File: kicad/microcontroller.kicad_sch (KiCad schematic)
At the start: 10 parts, among them J601 AVR-ISP-6, U601 ATtiny1634-S

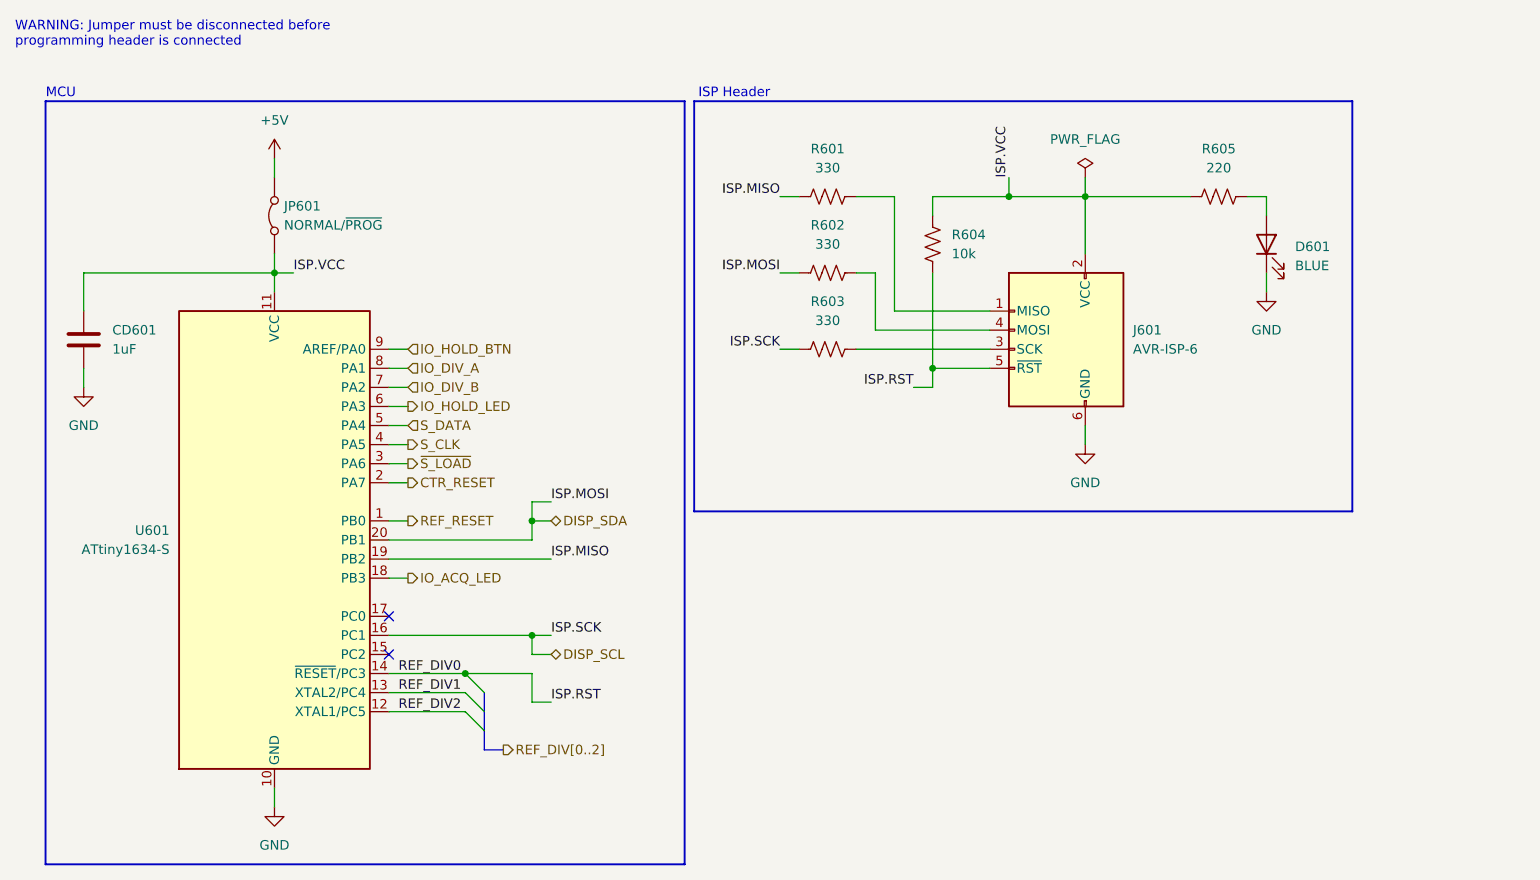
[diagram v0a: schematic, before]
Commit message: rework isp header, update pinout
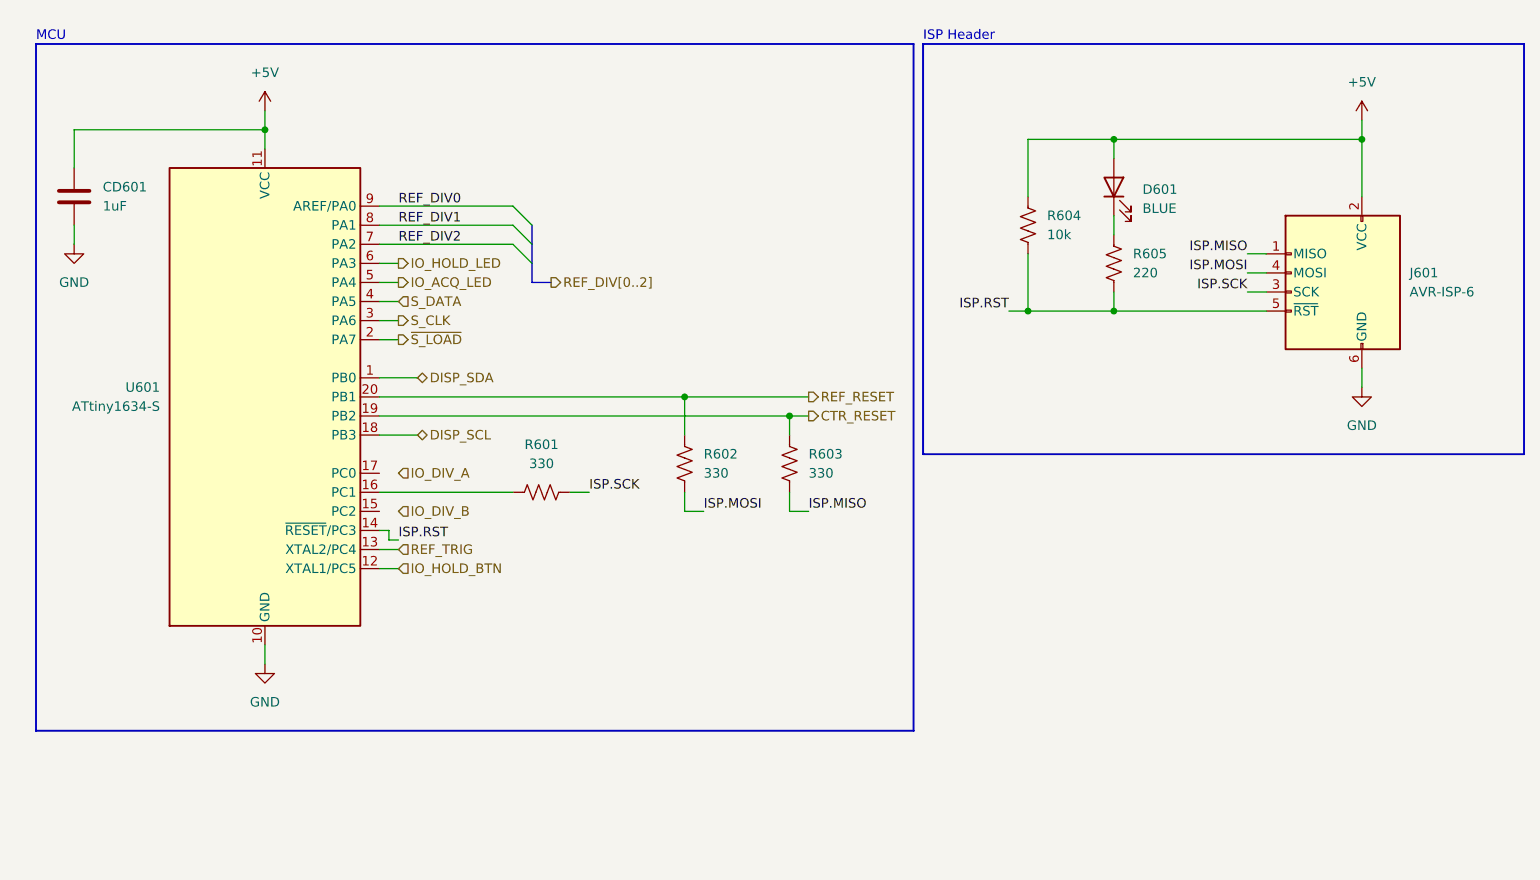
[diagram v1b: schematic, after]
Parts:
- removed JP601: NORMAL/~{PROG}, Custom:TestPoint_2Pads_Pitch2.54mm_Drill0.8mm_Fix, symbol Jumper:Jumper_2_Bridged
- renumbered R603 to R601, R601 to R602, R602 to R603
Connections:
- net +5V: now also CD601.1, D601.2 (A), J601.2 (VCC), R604.1, U601.11 (VCC)
- net CTR_RESET: now also R603.2, U601.19 (PB2); no longer U601.2 (PA7)
- net DISP_SCL: now also U601.18 (PB3); no longer R601.1, U601.16 (PC1)
- net DISP_SDA: now also U601.1 (PB0); no longer R603.1, U601.20 (PB1)
- net GND: no longer D601.1 (K)
- net IO_ACQ_LED: now also U601.5 (PA4); no longer U601.18 (PB3)
- net IO_DIV_A: no longer U601.8 (PA1)
- net IO_DIV_B: no longer U601.7 (PA2)
- net IO_HOLD_BTN: now also U601.12 (XTAL1/PC5); no longer U601.9 (AREF/PA0)
- net ISP.MISO: now also J601.1 (MISO), R603.1; no longer R602.1, U601.19 (PB2)
- net ISP.RST: now also R605.1
- net REF_DIV1: now also U601.8 (PA1); no longer U601.13 (XTAL2/PC4)
- net REF_DIV2: now also U601.7 (PA2); no longer U601.12 (XTAL1/PC5)
- net REF_RESET: now also R602.1, U601.20 (PB1); no longer U601.1 (PB0)
- net S_CLK: now also U601.3 (PA6); no longer U601.4 (PA5)
- net S_DATA: now also U601.4 (PA5); no longer U601.5 (PA4)
- net ~{S_LOAD}: now also U601.2 (PA7); no longer U601.3 (PA6)
- net ISP.MOSI: now reaches R602.2
- net ISP.MOSI: now also J601.4 (MOSI); no longer J601.1 (MISO)
- net at R601.2: now also U601.16 (PC1); no longer J601.3 (SCK)
- net at R605.2: now also D601.1 (K); no longer D601.2 (A)
- removed net ISP.VCC: CD601.1, J601.2 (VCC), R604.1, R605.1, U601.11 (VCC)
- new net ISP.SCK: J601.3 (SCK), R601.1
- new net REF_DIV0: U601.9 (AREF/PA0)
- new net REF_TRIG: U601.13 (XTAL2/PC4)
- no-connect marks 2 -> 0
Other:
- note removed: "WARNING: Jumper must be disconnected before programming header is connected"
- moved on the sheet: CD601, D601, J601, R601, R602, R603, R604, R605, U601

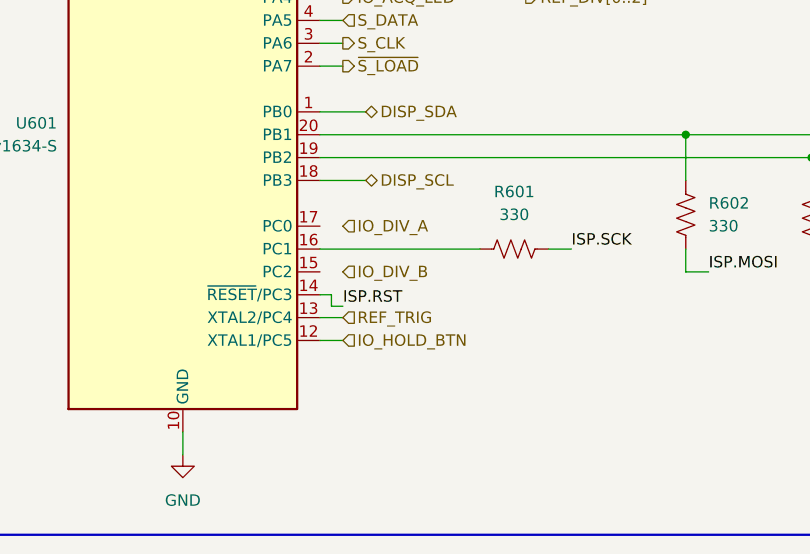
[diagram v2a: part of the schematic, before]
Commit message: swap encoder for two buttons, assign channel select pin
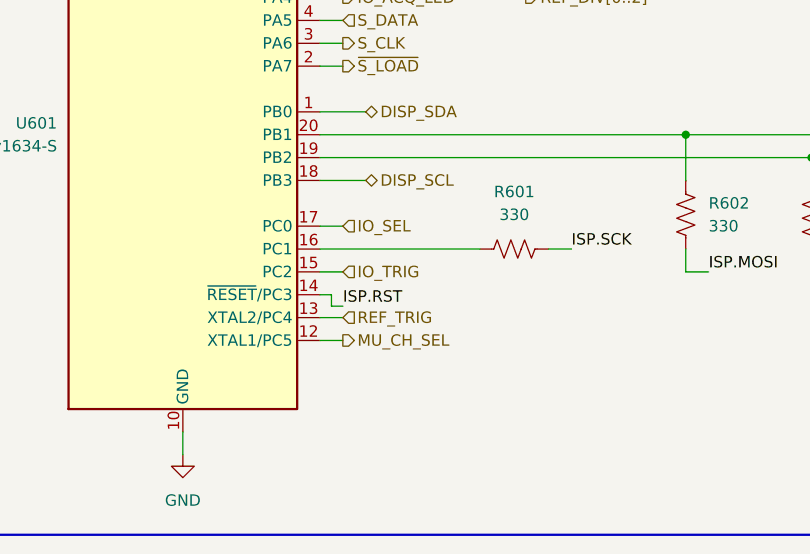
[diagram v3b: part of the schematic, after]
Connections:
- net IO_TRIG: now reaches U601.15 (PC2)
- net IO_SEL: now reaches U601.17 (PC0)
- net IO_HOLD_BTN renamed MU_CH_SEL
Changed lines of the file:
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@@
+	(wire
+		(pts
+			(xy 62.23 74.93) (xy 64.77 74.93)
+		)
+		(stroke
+			(width 0)
+			(type default)
+		)
+	)
 	(wire
 		(pts
@@
 		(pts
 			(xy 62.23 87.63) (xy 64.77 87.63)
+		)
+		(stroke
+			(width 0)
+			(type default)
+		)
+	)
+	(wire
+		(pts
+			(xy 62.23 80.01) (xy 64.77 80.01)
 		)
 		(stroke
@@
 		)
 	)
+	(hierarchical_label "MU_CH_SEL"
+		(shape output)
+		(at 64.77 87.63 0)
+		(effects
+			(font
+				(size 1.27 1.27)
+			)
+			(justify left)
+		)
+	)
 	(hierarchical_label "S_CLK"
 		(shape output)
@@
 		)
 	)
-	(hierarchical_label "IO_DIV_B"
+	(hierarchical_label "IO_TRIG"
 		(shape input)
 		(at 64.77 80.01 0)
@@
 		)
 	)
-	(hierarchical_label "IO_HOLD_BTN"
-		(shape input)
-		(at 64.77 87.63 0)
-		(effects
-			(font
-				(size 1.27 1.27)
-			)
-			(justify left)
-		)
-	)
 	(hierarchical_label "REF_DIV[0..2]"
 		(shape output)
@@
 		)
 	)
-	(hierarchical_label "IO_DIV_A"
+	(hierarchical_label "IO_SEL"
 		(shape input)
 		(at 64.77 74.93 0)

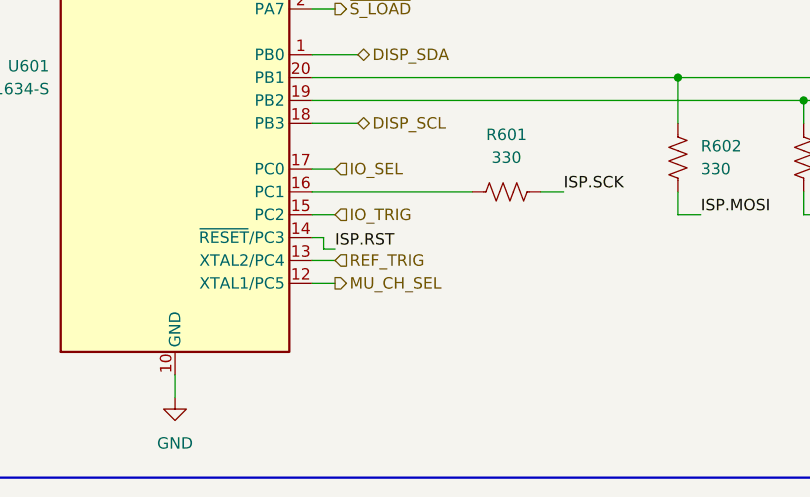
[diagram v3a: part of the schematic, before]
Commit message: rework frontend, channel gating
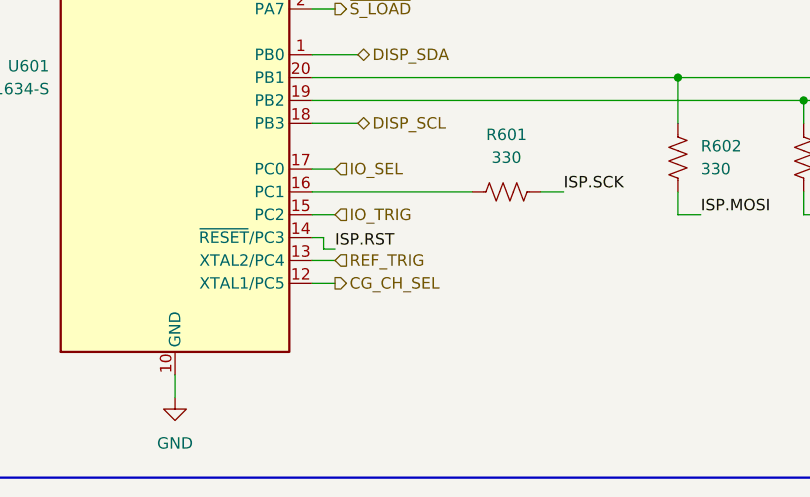
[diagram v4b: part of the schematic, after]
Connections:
- net MU_CH_SEL renamed CG_CH_SEL
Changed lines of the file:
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@@
 		)
 	)
-	(hierarchical_label "MU_CH_SEL"
+	(hierarchical_label "CG_CH_SEL"
 		(shape output)
 		(at 64.77 87.63 0)

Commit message: replace alum caps with ceramics, change mpn labeling
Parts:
- CD601: MPN (none) -> 0402ZD105KAT2A; Supplier https://www.digikey.com/en/products/detail/kyocera-avx/0402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 -> (none)
- D601: MPN (none) -> E1221NB--05D000814U1930; Supplier https://www.digikey.com/en/products/detail/harvatek-corpora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 -> (none)
- J601: Supplier Generic -> (none)
- R601, R602, R603: MPN (none) -> RC0402JR-13330RL; Supplier https://www.digikey.com/en/products/detail/yageo/RC0402JR-1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 -> (none)
- R604: MPN (none) -> RC0402JR-1310KL; Supplier https://www.digikey.com/en/products/detail/yageo/RC0402JR-1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 -> (none)
- R605: MPN (none) -> RC0402JR-13220RL; Supplier https://www.digikey.com/en/products/detail/yageo/RC0402JR-1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 -> (none)
- U601: MPN (none) -> ATTINY1634-SU; Supplier https://www.digikey.com/en/products/detail/microchip-techno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 -> (none)
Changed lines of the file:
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@@
 			)
 		)
-		(property "Supplier" "Generic"
+		(property "Supplier" ""
 			(at 190.5 50.8 0)
 			(effects
@@
 			)
 		)
-		(property "Supplier" "https://www.digikey.com/en/products/detail/yageo/RC0402JR-13220RL/14008194"
+		(property "Supplier" ""
 			(at 160.02 46.99 90)
+			(effects
+				(font
+					(size 1.27 1.27)
+				)
+				(hide yes)
+			)
+		)
+		(property "MPN" "RC0402JR-13220RL"
+			(at 160.02 46.99 0)
 			(effects
 				(font
@@
 			)
 		)
-		(property "Supplier" "https://www.digikey.com/en/products/detail/yageo/RC0402JR-13330RL/14008183"
+		(property "Supplier" ""
 			(at 102.87 73.66 90)
+			(effects
+				(font
+					(size 1.27 1.27)
+				)
+				(hide yes)
+			)
+		)
+		(property "MPN" "RC0402JR-13330RL"
+			(at 102.87 73.66 0)
 			(effects
 				(font
@@
 			)
 		)
-		(property "Supplier" "https://www.digikey.com/en/products/detail/kyocera-avx/0402ZD105KAT2A/1545026"
+		(property "Supplier" ""
+			(at 21.59 38.1 0)
+			(effects
+				(font
+					(size 1.27 1.27)
+				)
+				(hide yes)
+			)
+		)
+		(property "MPN" "0402ZD105KAT2A"
 			(at 21.59 38.1 0)
 			(effects
@@
 			)
 		)
-		(property "Supplier" "https://www.digikey.com/en/products/detail/yageo/RC0402JR-13330RL/14008183"
+		(property "Supplier" ""
 			(at 116.84 73.66 90)
+			(effects
+				(font
+					(size 1.27 1.27)
+				)
+				(hide yes)
+			)
+		)
+		(property "MPN" "RC0402JR-13330RL"
+			(at 116.84 73.66 0)
 			(effects
 				(font
@@
 			)
 		)
-		(property "Supplier" "https://www.digikey.com/en/products/detail/yageo/RC0402JR-13330RL/14008183"
+		(property "Supplier" ""
+			(at 83.82 77.47 90)
+			(effects
+				(font
+					(size 1.27 1.27)
+				)
+				(hide yes)
+			)
+		)
+		(property "MPN" "RC0402JR-13330RL"
 			(at 83.82 77.47 90)
 			(effects
@@
 			)
 		)
-		(property "Supplier" "https://www.digikey.com/en/products/detail/yageo/RC0402JR-1310KL/13694115"
+		(property "Supplier" ""
+			(at 148.59 41.91 0)
+			(effects
+				(font
+					(size 1.27 1.27)
+				)
+				(hide yes)
+			)
+		)
+		(property "MPN" "RC0402JR-1310KL"
 			(at 148.59 41.91 0)
 			(effects
@@
 			)
 		)
-		(property "Supplier" "https://www.digikey.com/en/products/detail/microchip-technology/ATTINY1634-SU/3128695"
+		(property "Supplier" ""
+			(at 46.99 64.77 0)
+			(effects
+				(font
+					(size 1.27 1.27)
+				)
+				(hide yes)
+			)
+		)
+		(property "MPN" "ATTINY1634-SU"
 			(at 46.99 64.77 0)
 			(effects
@@
 			)
 		)
-		(property "Supplier" "https://www.digikey.com/en/products/detail/harvatek-corporation/E1221NB-05D000814U1930/18165804"
+		(property "Supplier" ""
 			(at 160.02 36.83 90)
 			(effects
+				(font
+					(size 1.27 1.27)
+				)
+				(hide yes)
+			)
+		)
+		(property "MPN" "E1221NB--05D000814U1930"
+			(at 160.02 36.83 90)
+			(effects

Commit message: assign references
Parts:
- renumbered CD601 to CD701, D601 to D701, J601 to J701, R601 to R701, R602 to R702, R603 to R703, R604 to R704, R605 to R705, U601 to U701
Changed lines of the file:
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@@
 		(dnp no)
 		(fields_autoplaced yes)
-		(property "Reference" "J601"
+		(property "Reference" "J701"
 			(at 199.39 48.2599 0)
 			(effects
@@
 			(project ""
 				(path "/62339e8b-4e00-440f-8d81-4472a4f50c26/2a521c09-f149-46cd-82ca-3e519b54aa9b"
-					(reference "J601")
+					(reference "J701")
 					(unit 1)
 				)
@@
 		(dnp no)
 		(fields_autoplaced yes)
-		(property "Reference" "R605"
+		(property "Reference" "R705"
 			(at 162.56 45.7199 0)
 			(effects
@@
 			(project "frequency_counter"
 				(path "/62339e8b-4e00-440f-8d81-4472a4f50c26/2a521c09-f149-46cd-82ca-3e519b54aa9b"
-					(reference "R605")
+					(reference "R705")
 					(unit 1)
 				)
@@
 		(dnp no)
 		(fields_autoplaced yes)
-		(property "Reference" "R602"
+		(property "Reference" "R702"
 			(at 105.41 72.3899 0)
 			(effects
@@
 			(project "frequency_counter"
 				(path "/62339e8b-4e00-440f-8d81-4472a4f50c26/2a521c09-f149-46cd-82ca-3e519b54aa9b"
-					(reference "R602")
+					(reference "R702")
 					(unit 1)
 				)
@@
 		(dnp no)
 		(fields_autoplaced yes)
-		(property "Reference" "#PWR0601"
+		(property "Reference" "#PWR0701"
 			(at 21.59 50.8 0)
 			(effects
@@
 			(project "frequency_counter"
 				(path "/62339e8b-4e00-440f-8d81-4472a4f50c26/2a521c09-f149-46cd-82ca-3e519b54aa9b"
-					(reference "#PWR0601")
+					(reference "#PWR0701")
 					(unit 1)
 				)
@@
 		(dnp no)
 		(fields_autoplaced yes)
-		(property "Reference" "#PWR0603"
+		(property "Reference" "#PWR0703"
 			(at 46.99 106.68 0)
 			(effects
@@
 			(project ""
 				(path "/62339e8b-4e00-440f-8d81-4472a4f50c26/2a521c09-f149-46cd-82ca-3e519b54aa9b"
-					(reference "#PWR0603")
+					(reference "#PWR0703")
 					(unit 1)
 				)
@@
 		(dnp no)
 		(fields_autoplaced yes)
-		(property "Reference" "CD601"
+		(property "Reference" "CD701"
 			(at 25.4 36.8299 0)
 			(effects
@@
 			(project "frequency_counter"
 				(path "/62339e8b-4e00-440f-8d81-4472a4f50c26/2a521c09-f149-46cd-82ca-3e519b54aa9b"
-					(reference "CD601")
+					(reference "CD701")
 					(unit 1)
 				)
@@
 		(dnp no)
 		(fields_autoplaced yes)
-		(property "Reference" "#PWR0602"
+		(property "Reference" "#PWR0702"
 			(at 46.99 30.48 0)
 			(effects
@@
 			(project "frequency_counter"
 				(path "/62339e8b-4e00-440f-8d81-4472a4f50c26/2a521c09-f149-46cd-82ca-3e519b54aa9b"
-					(reference "#PWR0602")
+					(reference "#PWR0702")
 					(unit 1)
 				)
@@
 		(dnp no)
 		(fields_autoplaced yes)
-		(property "Reference" "R603"
+		(property "Reference" "R703"
 			(at 119.38 72.3899 0)
 			(effects
@@
 			(project "frequency_counter"
 				(path "/62339e8b-4e00-440f-8d81-4472a4f50c26/2a521c09-f149-46cd-82ca-3e519b54aa9b"
-					(reference "R603")
+					(reference "R703")
 					(unit 1)
 				)
@@
 		(dnp no)
 		(fields_autoplaced yes)
-		(property "Reference" "#PWR0604"
+		(property "Reference" "#PWR0704"
 			(at 193.04 31.75 0)
 			(effects
@@
 			(project "frequency_counter"
 				(path "/62339e8b-4e00-440f-8d81-4472a4f50c26/2a521c09-f149-46cd-82ca-3e519b54aa9b"
-					(reference "#PWR0604")
+					(reference "#PWR0704")
 					(unit 1)
 				)
@@
 		(dnp no)
 		(fields_autoplaced yes)
-		(property "Reference" "R601"
+		(property "Reference" "R701"
 			(at 83.82 71.12 90)
 			(effects
@@
 			(project "frequency_counter"
 				(path "/62339e8b-4e00-440f-8d81-4472a4f50c26/2a521c09-f149-46cd-82ca-3e519b54aa9b"
-					(reference "R601")
+					(reference "R701")
 					(unit 1)
 				)
@@
 		(dnp no)
 		(fields_autoplaced yes)
-		(property "Reference" "#PWR0605"
+		(property "Reference" "#PWR0705"
 			(at 193.04 69.85 0)
 			(effects
@@
 			(project "frequency_counter"
 				(path "/62339e8b-4e00-440f-8d81-4472a4f50c26/2a521c09-f149-46cd-82ca-3e519b54aa9b"
-					(reference "#PWR0605")
+					(reference "#PWR0705")
 					(unit 1)
 				)
@@
 		(dnp no)
 		(fields_autoplaced yes)
-		(property "Reference" "R604"
+		(property "Reference" "R704"
 			(at 151.13 40.6399 0)
 			(effects
@@
 			(project "frequency_counter"
 				(path "/62339e8b-4e00-440f-8d81-4472a4f50c26/2a521c09-f149-46cd-82ca-3e519b54aa9b"
-					(reference "R604")
+					(reference "R704")
 					(unit 1)
 				)
@@
 		(dnp no)
 		(fields_autoplaced yes)
-		(property "Reference" "U601"
+		(property "Reference" "U701"
 			(at 33.02 63.4999 0)
 			(effects
@@
 			(project ""
 				(path "/62339e8b-4e00-440f-8d81-4472a4f50c26/2a521c09-f149-46cd-82ca-3e519b54aa9b"
-					(reference "U601")
+					(reference "U701")
 					(unit 1)
 				)
@@
 		(dnp no)
 		(fields_autoplaced yes)
-		(property "Reference" "D601"
+		(property "Reference" "D701"
 			(at 163.83 37.1474 90)
 			(effects
@@
 			(project "frequency_counter"
 				(path "/62339e8b-4e00-440f-8d81-4472a4f50c26/2a521c09-f149-46cd-82ca-3e519b54aa9b"
-					(reference "D601")
-					(unit 1)
-				)
+					(reference "D701")
+					(unit 1)
+				)
